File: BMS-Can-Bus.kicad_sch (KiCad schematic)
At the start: 58 parts, among them J1 Conn_01x05, J2 Conn_01x02, Q1 dfsg1, Q2 dsg2, Q3 Q_PMOS_GSD, Q4 Q_PMOS_GSD, Q5 Q_PMOS_GSD, Q6 Q_PMOS_GSD, Q7 chg1, Q8 chg2, U1 BQ76952PFB, U2 STM32F103C8Tx, U4 SN65HVD230

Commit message: Add files via upload
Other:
- company: Electric Vehicle Battery Management System -> Battery Management System
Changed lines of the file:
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@@
 		(title "BMS - CAN Bus")
 		(rev "1.0")
-		(company "Electric Vehicle Battery Management System")
-		(comment 1 "100A Electric Vehicle Battery Management System")
+		(company "Battery Management System")
+		(comment 1 "5A  Battery Management System")
 		(comment 2 "Designed by Hasan Berk Dasar")
 	)

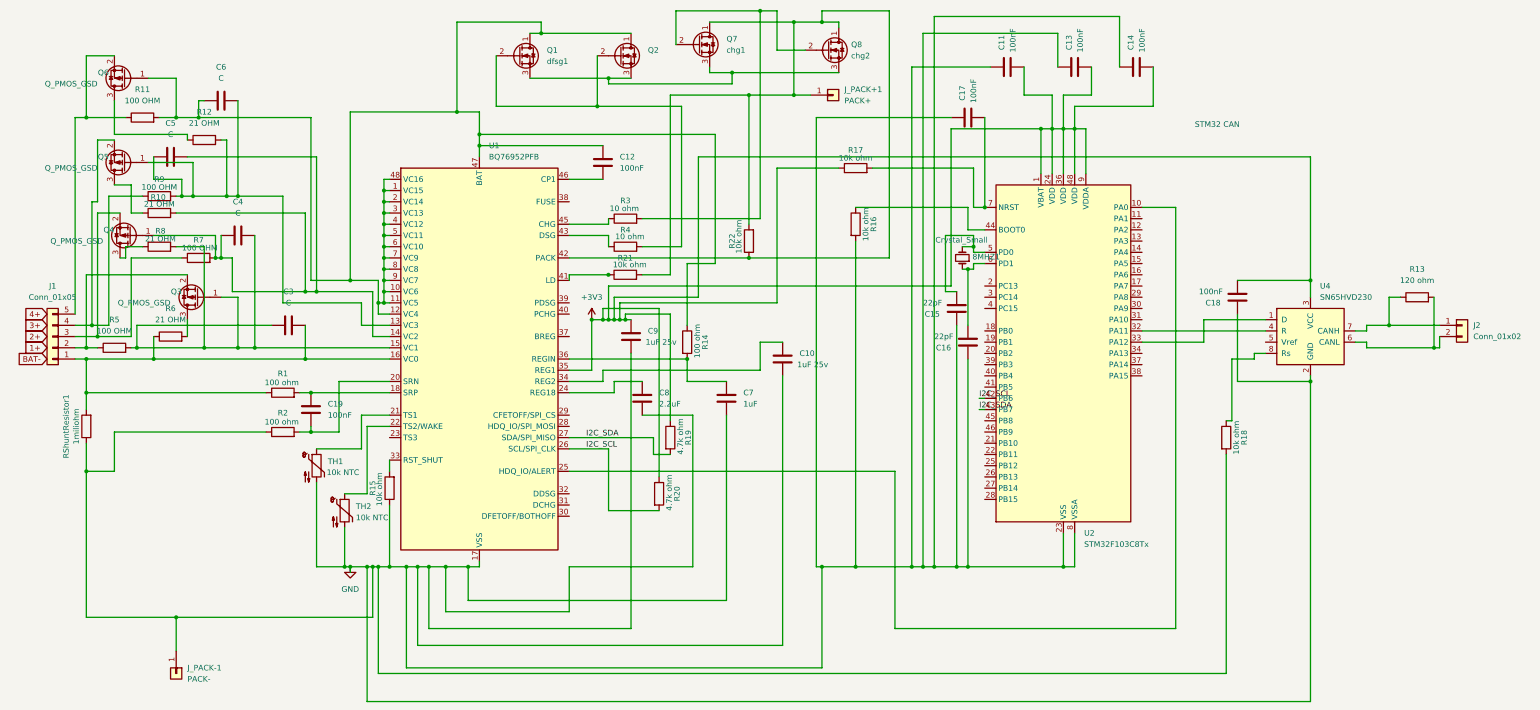
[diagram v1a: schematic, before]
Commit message: ERC warnning
Known open items: 2 ERC warnings remain unresolved (a GND net junction and the LD pin pull-up connection near R21) — likely a wire/grid-snap issue in the schematic editor that I couldn't fully trace. Flagging as a known limitation for this learning-stage design.
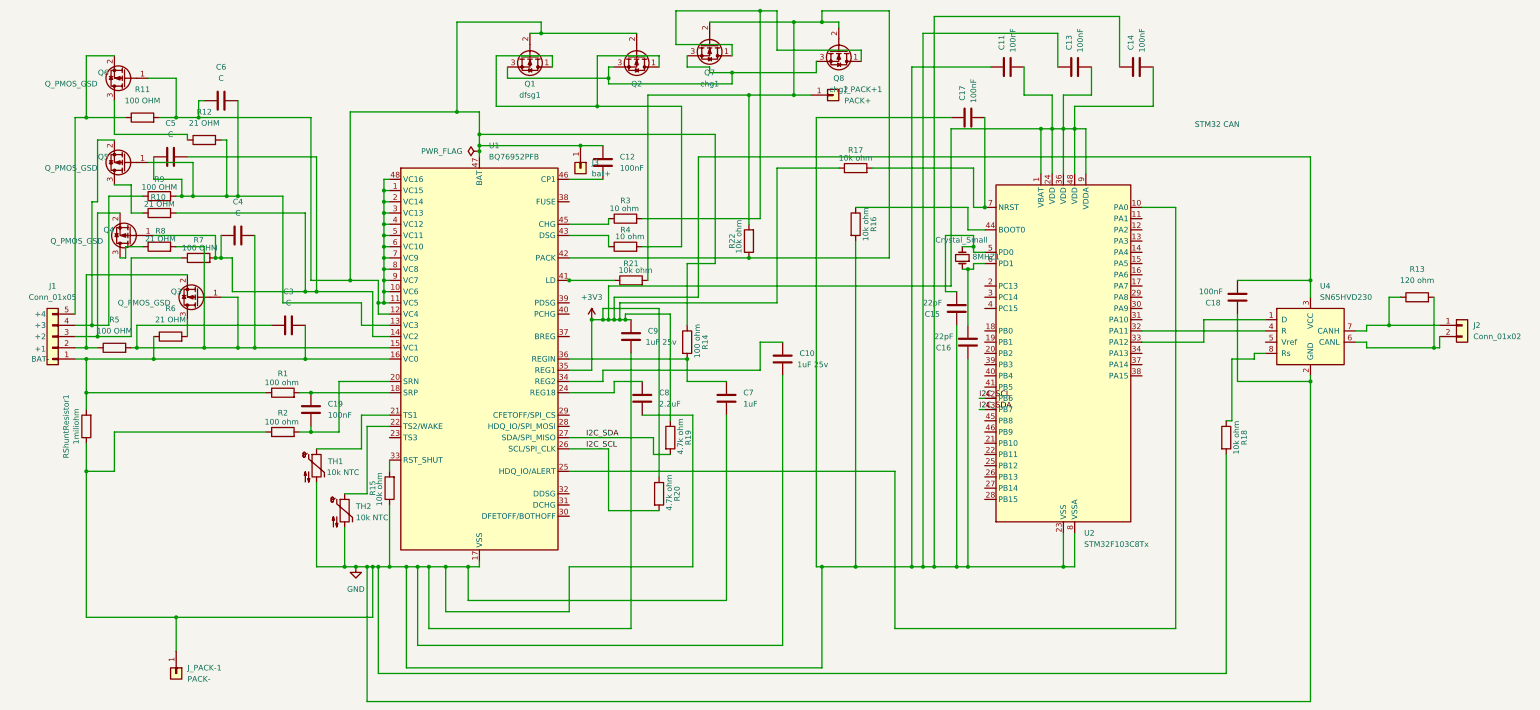
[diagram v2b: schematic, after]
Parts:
- added J3: bat+, MountingHole:MountingHole_3.2mm_M3_Pad, symbol Connector_Generic:Conn_01x01
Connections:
- net at C12.2, C6.1, Q6.1 (G)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: now also Q1.2 (G), Q2.2 (G), J3.1 (Pin_1); no longer Q1.1 (D), Q2.1 (D)
- net at J_PACK+1.1 (Pin_1), R22.1, R22.2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: now also Q7.2 (G), Q8.2 (G), R21.2; no longer Q7.1 (D), Q8.1 (D)
- new net: Q1.1 (D), Q2.1 (D), R4.2
- new net: Q7.1 (D), Q8.1 (D), R3.2
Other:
- note added: "+1"
- note added: "+2"
- note added: "+3"
- note added: "+4"
- note added: "BAT-"
- moved on the sheet: Q1, Q2, Q7, Q8, R21
